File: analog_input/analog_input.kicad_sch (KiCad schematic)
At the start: 18 parts, among them J1 Port 1, J2 Port 2, U1 C226S, U2 INA2181, U3 C226S

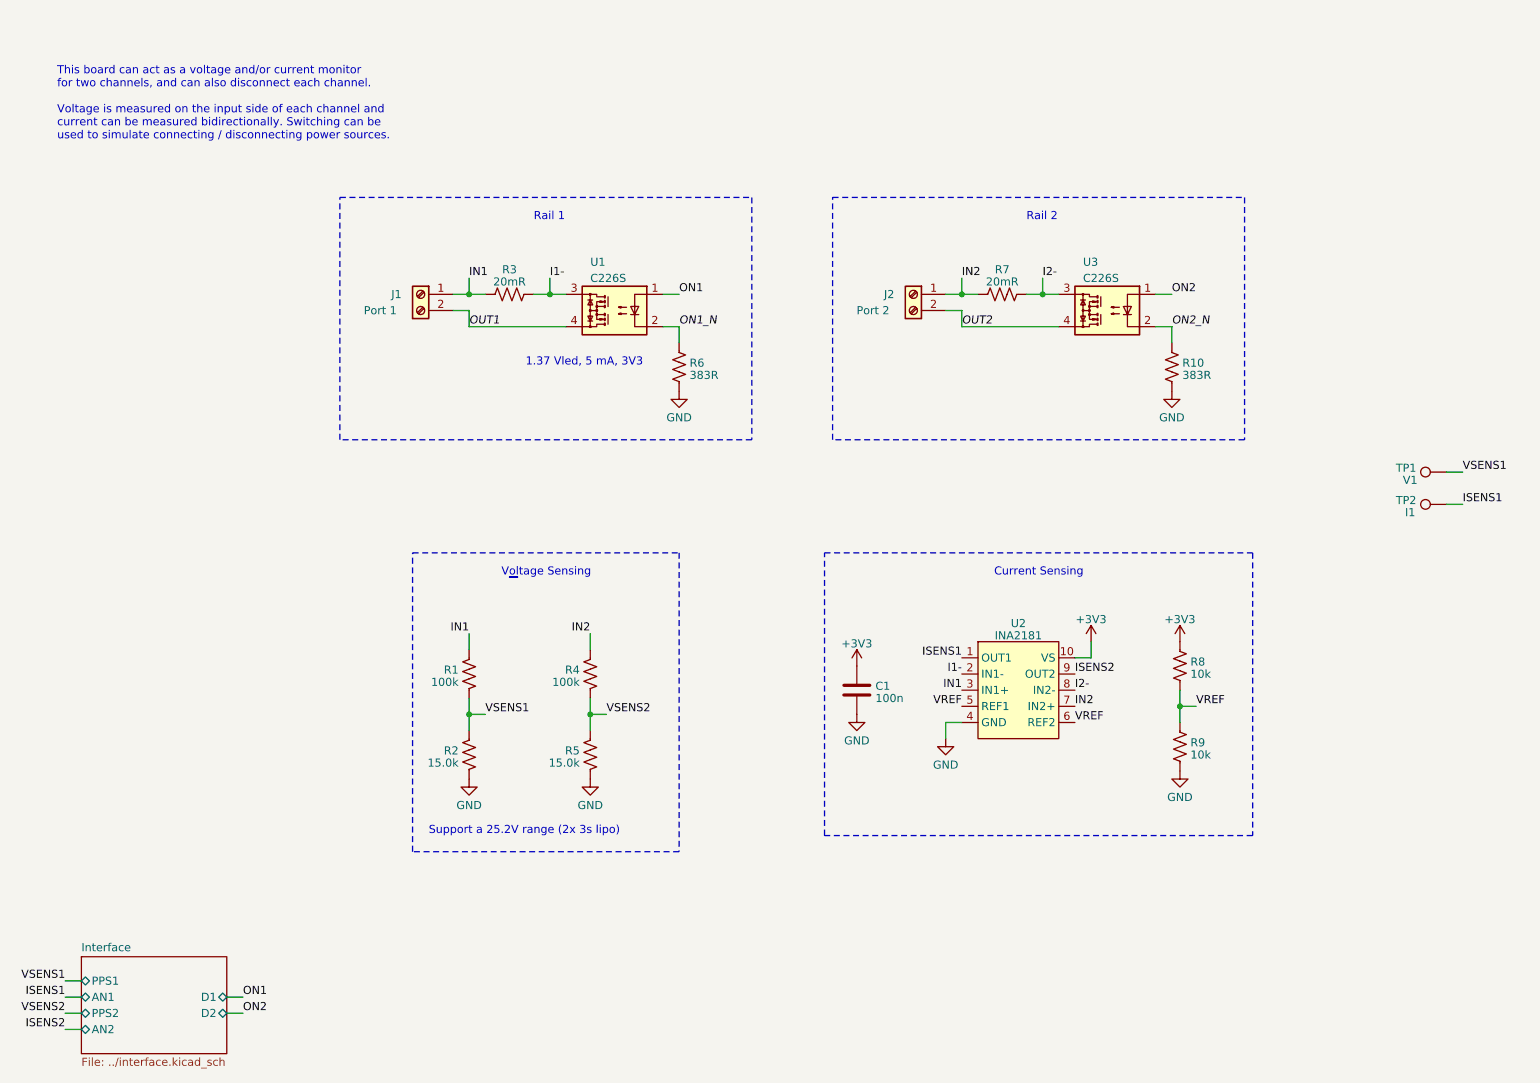
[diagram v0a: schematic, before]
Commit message: Address review comments, finish routing HILT main board
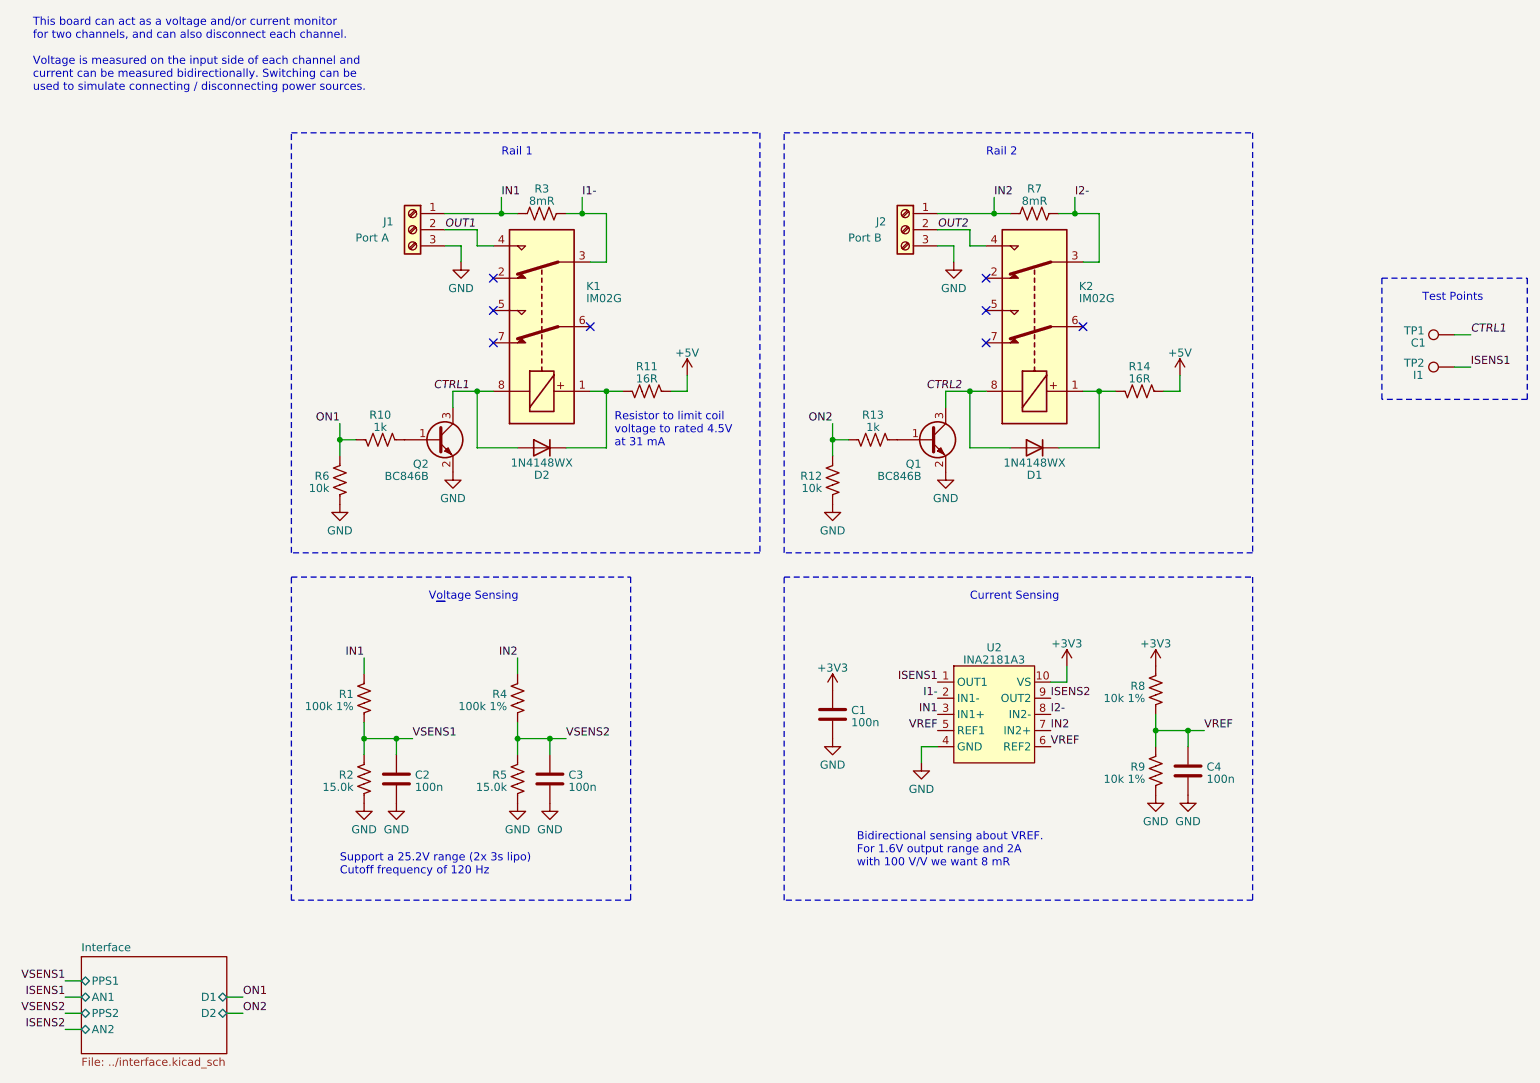
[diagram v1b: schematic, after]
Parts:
- removed J1: Port 1, TerminalBlock_Phoenix:TerminalBlock_Phoenix_PT-1,5-2-5.0-H_1x02_P5.00mm_Horizontal, symbol Connector:Screw_Terminal_01x02
- removed J2: Port 2, TerminalBlock_Phoenix:TerminalBlock_Phoenix_PT-1,5-2-5.0-H_1x02_P5.00mm_Horizontal, symbol Connector:Screw_Terminal_01x02
- removed U1, U3: C226S, Package_SO:SO-4_4.4x3.9mm_P2.54mm, symbol hil:C226S
- added C2, C3, C4: 100n, Capacitor_SMD:C_0805_2012Metric_Pad1.18x1.45mm_HandSolder, symbol Device:C
- added D1, D2: 1N4148WX, Diode_SMD:D_SOD-323_HandSoldering, symbol Diode:1N4148WT
- added J1: Port A, TerminalBlock_Phoenix:TerminalBlock_Phoenix_PT-1,5-3-3.5-H_1x03_P3.50mm_Horizontal, symbol Connector:Screw_Terminal_01x03
- added J2: Port B, TerminalBlock_Phoenix:TerminalBlock_Phoenix_PT-1,5-3-3.5-H_1x03_P3.50mm_Horizontal, symbol Connector:Screw_Terminal_01x03
- added K1, K2: IM02G, Relay_SMD:Relay_2P2T_10x6mm_TE_IMxxG, symbol Relay:IM02
- added Q1, Q2: BC846B, Package_TO_SOT_SMD:SOT-23, symbol Transistor_BJT:BC846
- added R11, R14: 16R, Resistor_SMD:R_0805_2012Metric_Pad1.20x1.40mm_HandSolder, symbol Device:R_US
- added R12: 10k, Resistor_SMD:R_0805_2012Metric_Pad1.20x1.40mm_HandSolder, symbol Device:R_US
- added R13: 1k, Resistor_SMD:R_0805_2012Metric_Pad1.20x1.40mm_HandSolder, symbol Device:R_US
- R1, R4: value 100k -> 100k 1%
- R10: value 383R -> 1k
- R3, R7: value 20mR -> 8mR
- R6: value 383R -> 10k
- R8, R9: value 10k -> 10k 1%
- TP1: value V1 -> C1
- U2: value INA2181 -> INA2181A3
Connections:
- net ON1_N is gone; now on net GND: R6.1
- net GND: now also C2.2, C3.2, C4.2, J1.3 (Pin_3), J2.3 (Pin_3), Q1.2 (E), Q2.2 (E), R12.1; no longer R10.2, R6.2
- net I1-: now also K1.3
- net I2-: now also K2.3
- net IN1: now also J1.1 (Pin_1)
- net IN2: now also J2.1 (Pin_1)
- net ON1: now also R10.2, R6.2
- net ON2: now also R12.2, R13.2
- net OUT1: now also J1.2 (Pin_2), K1.4
- net OUT2: now also J2.2 (Pin_2), K2.4
- net VREF: now also C4.1
- net VSENS1: now also C2.1; no longer TP1.1
- net VSENS2: now also C3.1
- net ON2_N: no longer names the net of R10.1
- net ON2_N: now also Q2.1 (B)
- new net: D1.1 (K), K2.1, R14.2
- new net: Q1.1 (B), R13.1
- new net: D2.1 (K), K1.1, R11.2
- new net +5V: R11.1, R14.1
- new net CTRL1: D2.2 (A), K1.8, Q2.3 (C), TP1.1
- new net CTRL2: D1.2 (A), K2.8, Q1.3 (C)
- no-connect marks 0 -> 8
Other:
- note added: "Bidirectional sensing about VREF. For 1.6V output range and 2A with 100 V/V we want 8 mR"
- note added: "Resistor to limit coil voltage to rated 4.5V at 31 mA"
- note added: "Support a 25.2V range (2x 3s lipo) Cutoff frequency of 120 Hz"
- note added: "Test Points"
- note removed: "1.37 Vled, 5 mA, 3V3"
- note removed: "Support a 25.2V range (2x 3s lipo)"
- moved on the sheet: C1, R1, R2, R3, R4, R5, R7, R8, R9, TP1, U2
